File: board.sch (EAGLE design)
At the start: 130 parts, among them IC2 TPS61088RHLR, IC3 LMZ10501, Q1 IRFML8244TRPBF, Q2 IRFML8244TRPBF, Q3 IRFML8244TRPBF, Q4 IRFML8244TRPBF, Q5 IRFML8244TRPBF, U1 TB6612FNG, U3 STM32F405RG, U4 BMI088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

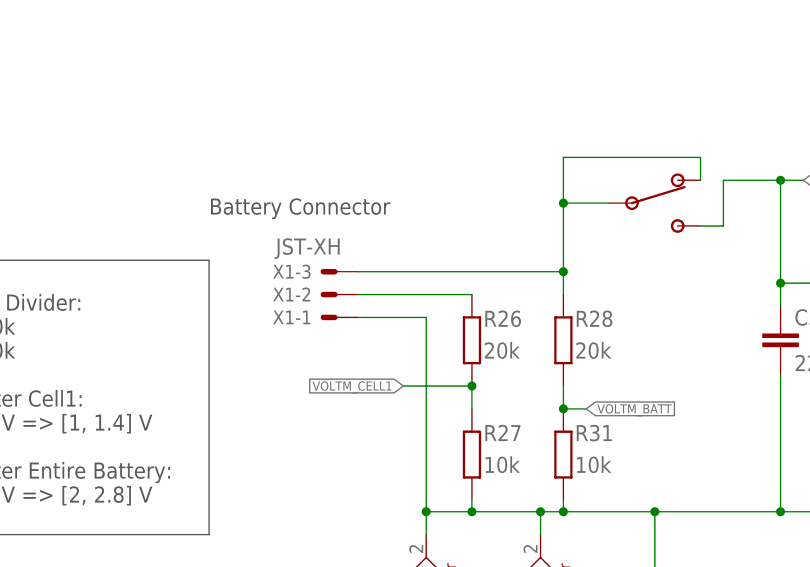
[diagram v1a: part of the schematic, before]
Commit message: 3D packages and footprint updates + board picture
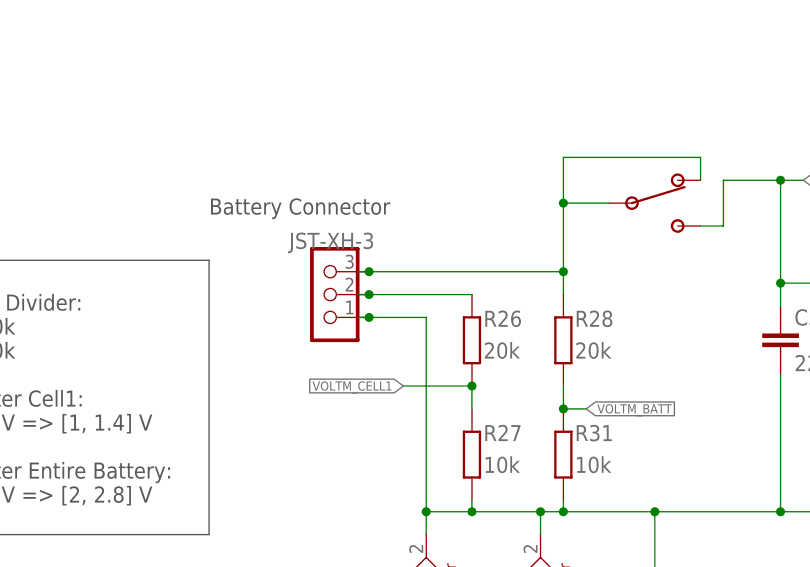
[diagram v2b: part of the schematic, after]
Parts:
- removed X1: JST-XH, JST XH Connectors:JST-XH-03-PIN-LONG-PAD
- added U$10: JST-XH-3, Isaks Bibliotek:JST-XH-3
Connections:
- net GND: now also U$10.1; no longer X1-1.S
- net N$33: now also U$10.2; no longer X1-2.S
- net N$38: now also U$10.3; no longer X1-3.S

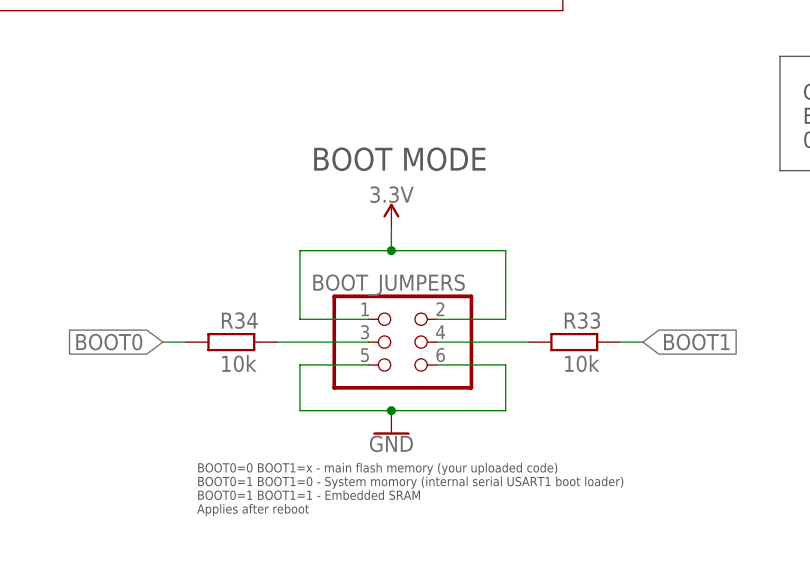
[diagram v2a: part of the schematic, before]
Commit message: 3D packages + component layout
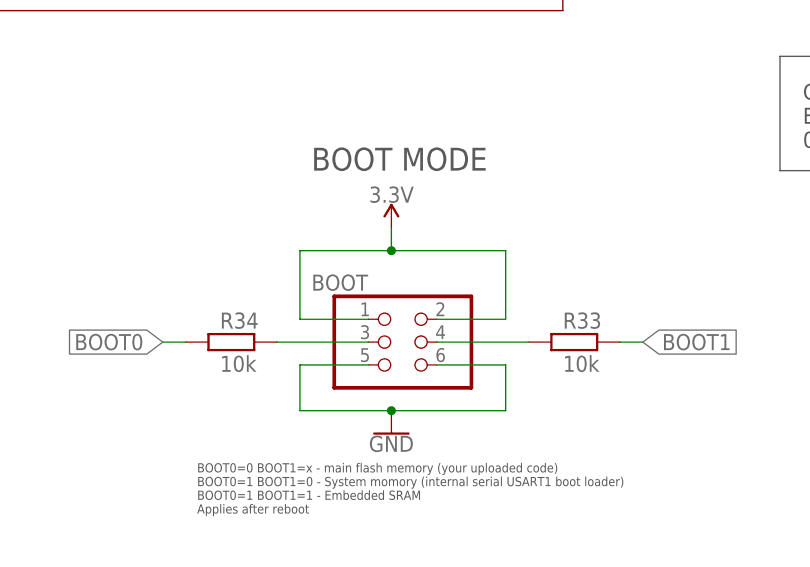
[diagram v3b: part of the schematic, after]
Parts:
- C31: RATING (none) -> X5R/X7R; V_RATING (none) -> 10V
- C32: RATING (none) -> X5R/X7R; V_RATING (none) -> 25V
- C33: V_RATING (none) -> 10v
- C_VC: RATING (none) -> X5R/X7R; V_RATING (none) -> 6.3V
- R23, RT: TOLERANCE (none) -> 1%
- renumbered BOOT_JUMPERS to BOOT
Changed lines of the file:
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@@
 <part name="R1" library="CASE-RCL" deviceset="R0603" device="" package3d_urn="urn:adsk.eagle:package:5332309/4" value="1.8k"/>
 <part name="R2" library="CASE-RCL" deviceset="R0603" device="" package3d_urn="urn:adsk.eagle:package:5332309/4" value="1.8k"/>
-<part name="RT" library="CASE-RCL" deviceset="R0603" device="" package3d_urn="urn:adsk.eagle:package:5332309/4" value="290k"/>
+<part name="RT" library="CASE-RCL" deviceset="R0603" device="" package3d_urn="urn:adsk.eagle:package:5332309/4" value="290k">
+<attribute name="TOLERANCE" value="1%"/>
+</part>
 <part name="RB" library="CASE-RCL" deviceset="R0603" device="" package3d_urn="urn:adsk.eagle:package:5332309/4" value="150k"/>
 <part name="C_IN" library="CASE-RCL" deviceset="C0805" device="" package3d_urn="urn:adsk.eagle:package:5332304/3" value="10u"/>
 <part name="C_OUT" library="CASE-RCL" deviceset="C0805" device="" package3d_urn="urn:adsk.eagle:package:5332304/3" value="10u"/>
-<part name="C_VC" library="CASE-RCL" deviceset="C0603" device="" package3d_urn="urn:adsk.eagle:package:5332305/5" value="470pF"/>
+<part name="C_VC" library="CASE-RCL" deviceset="C0603" device="" package3d_urn="urn:adsk.eagle:package:5332305/5" value="470pF">
+<attribute name="RATING" value="X5R/X7R"/>
+<attribute name="V_RATING" value="6.3V"/>
+</part>
 <part name="Q4" library="Isaks Bibliotek" library_urn="urn:adsk.eagle:library:11889733" deviceset="IRFML8244TRPBF" device="" package3d_urn="urn:adsk.eagle:package:12478112/1"/>
 <part name="Q3" library="Isaks Bibliotek" library_urn="urn:adsk.eagle:library:11889733" deviceset="IRFML8244TRPBF" device="" package3d_urn="urn:adsk.eagle:package:12478112/1"/>
@@
 <part name="S1" library="Isaks Bibliotek" library_urn="urn:adsk.eagle:library:11889733" deviceset="LMZ21701" device="" package3d_urn="urn:adsk.eagle:package:12971317/2"/>
 <part name="R_FBB" library="CASE-RCL" deviceset="R0603" device="" package3d_urn="urn:adsk.eagle:package:5332309/4" value="20k"/>
-<part name="C31" library="CASE-RCL" deviceset="C0603" device="" package3d_urn="urn:adsk.eagle:package:5332305/5" value="3300p"/>
+<part name="C31" library="CASE-RCL" deviceset="C0603" device="" package3d_urn="urn:adsk.eagle:package:5332305/5" value="3300p">
+<attribute name="RATING" value="X5R/X7R"/>
+<attribute name="V_RATING" value="10V"/>
+</part>
 <part name="GND21" library="Isaks Bibliotek" library_urn="urn:adsk.eagle:library:11889733" deviceset="GND" device=""/>
-<part name="C32" library="CASE-RCL" deviceset="C0805" device="" package3d_urn="urn:adsk.eagle:package:5332304/3" value="22u"/>
-<part name="R23" library="CASE-RCL" deviceset="R0603" device="" package3d_urn="urn:adsk.eagle:package:5332309/4" value="10k"/>
-<part name="C33" library="CASE-RCL" deviceset="C0805" device="" package3d_urn="urn:adsk.eagle:package:5332304/3" value="22u"/>
+<part name="C32" library="CASE-RCL" deviceset="C0805" device="" package3d_urn="urn:adsk.eagle:package:5332304/3" value="22u">
+<attribute name="RATING" value="X5R/X7R"/>
+<attribute name="V_RATING" value="25V"/>
+</part>
+<part name="R23" library="CASE-RCL" deviceset="R0603" device="" package3d_urn="urn:adsk.eagle:package:5332309/4" value="10k">
+<attribute name="TOLERANCE" value="1%"/>
+</part>
+<part name="C33" library="CASE-RCL" deviceset="C0805" device="" package3d_urn="urn:adsk.eagle:package:5332304/3" value="22u">
+<attribute name="V_RATING" value="10v"/>
+</part>
 <part name="SUPPLY14" library="Isaks Bibliotek" library_urn="urn:adsk.eagle:library:11889733" deviceset="5V" device=""/>
 <part name="R_FBT" library="CASE-RCL" deviceset="R0603" device="" package3d_urn="urn:adsk.eagle:package:5332309/4" value="105k"/>
@@
 <part name="GND34" library="Isaks Bibliotek" library_urn="urn:adsk.eagle:library:11889733" deviceset="GND" device=""/>
 <part name="SUPPLY27" library="Isaks Bibliotek" library_urn="urn:adsk.eagle:library:11889733" deviceset="3.3V" device=""/>
-<part name="BOOT_JUMPERS" library="CASE-Pinhead" deviceset="PINHD-2X3" device="" package3d_urn="urn:adsk.eagle:package:22462/2"/>
+<part name="BOOT" library="CASE-Pinhead" deviceset="PINHD-2X3" device="" package3d_urn="urn:adsk.eagle:package:22462/2"/>
 <part name="SUPPLY29" library="SparkFun-PowerSymbols" deviceset="3.3V" device=""/>
 <part name="GND36" library="SparkFun-PowerSymbols" deviceset="GND" device=""/>
@@
 <attribute name="NAME" x="173.99" y="288.0614" size="1.778" layer="95" rot="R180"/>
 <attribute name="VALUE" x="173.99" y="285.242" size="1.778" layer="96" rot="R180"/>
+<attribute name="TOLERANCE" x="176.53" y="285.75" size="1.778" layer="96" rot="R90" display="off"/>
 </instance>
 <instance part="RB" gate="G$1" x="176.53" y="270.51" smashed="yes" rot="R90" grouprefs="POWER_REGULATION">
@@
 <attribute name="NAME" x="161.036" y="273.939" size="1.778" layer="95" rot="R180"/>
 <attribute name="VALUE" x="162.306" y="268.859" size="1.778" layer="96" rot="R180"/>
+<attribute name="RATING" x="163.83" y="271.78" size="1.778" layer="96" display="off"/>
+<attribute name="V_RATING" x="163.83" y="271.78" size="1.778" layer="96" display="off"/>
 </instance>
 <instance part="Q4" gate="G$1" x="299.72" y="439.42" smashed="yes" grouprefs="EMITTERS">
@@
 <attribute name="NAME" x="124.714" y="348.361" size="1.778" layer="95"/>
 <attribute name="VALUE" x="124.714" y="343.281" size="1.778" layer="96"/>
+<attribute name="RATING" x="123.19" y="347.98" size="1.778" layer="96" display="off"/>
+<attribute name="V_RATING" x="123.19" y="347.98" size="1.778" layer="96" display="off"/>
 </instance>
 <instance part="GND21" gate="1" x="102.87" y="314.96" smashed="yes" grouprefs="POWER_REGULATION">
@@
 <attribute name="NAME" x="118.364" y="357.251" size="1.778" layer="95"/>
 <attribute name="VALUE" x="118.364" y="352.171" size="1.778" layer="96"/>
+<attribute name="RATING" x="116.84" y="356.87" size="1.778" layer="96" display="off"/>
+<attribute name="V_RATING" x="116.84" y="356.87" size="1.778" layer="96" display="off"/>
 </instance>
 <instance part="R23" gate="G$1" x="167.64" y="356.87" smashed="yes" rot="R90" grouprefs="POWER_REGULATION">
 <attribute name="NAME" x="170.18" y="358.3686" size="1.778" layer="95"/>
 <attribute name="VALUE" x="170.18" y="354.838" size="1.778" layer="96"/>
+<attribute name="TOLERANCE" x="167.64" y="356.87" size="1.778" layer="96" rot="R90" display="off"/>
 </instance>
 <instance part="C33" gate="G$1" x="196.85" y="356.87" smashed="yes" grouprefs="POWER_REGULATION">
 <attribute name="NAME" x="198.374" y="357.251" size="1.778" layer="95"/>
 <attribute name="VALUE" x="198.374" y="352.171" size="1.778" layer="96"/>
+<attribute name="V_RATING" x="196.85" y="356.87" size="1.778" layer="96" display="off"/>
 </instance>
 <instance part="SUPPLY14" gate="G$1" x="196.85" y="365.76" smashed="yes" grouprefs="POWER_REGULATION">
@@
 <attribute name="VALUE" x="525.78" y="322.834" size="1.778" layer="96" align="bottom-center"/>
 </instance>
-<instance part="BOOT_JUMPERS" gate="A" x="449.58" y="218.44" smashed="yes" grouprefs="MICROCONTROLLER">
+<instance part="BOOT" gate="A" x="449.58" y="218.44" smashed="yes" grouprefs="MICROCONTROLLER">
 <attribute name="NAME" x="440.69" y="224.155" size="1.778" layer="95"/>
 <attribute name="VALUE" x="443.23" y="210.82" size="1.778" layer="96"/>
@@
 </segment>
 <segment>
-<pinref part="BOOT_JUMPERS" gate="A" pin="5"/>
+<pinref part="BOOT" gate="A" pin="5"/>
 <wire x1="447.04" y1="215.9" x2="439.42" y2="215.9" width="0.1524" layer="91" grouprefs="MICROCONTROLLER"/>
 <wire x1="439.42" y1="215.9" x2="439.42" y2="210.82" width="0.1524" layer="91" grouprefs="MICROCONTROLLER"/>
 <wire x1="439.42" y1="210.82" x2="449.58" y2="210.82" width="0.1524" layer="91" grouprefs="MICROCONTROLLER"/>
 <pinref part="GND36" gate="1" pin="GND"/>
-<pinref part="BOOT_JUMPERS" gate="A" pin="6"/>
+<pinref part="BOOT" gate="A" pin="6"/>
 <wire x1="454.66" y1="215.9" x2="462.28" y2="215.9" width="0.1524" layer="91" grouprefs="MICROCONTROLLER"/>
 <wire x1="462.28" y1="215.9" x2="462.28" y2="210.82" width="0.1524" layer="91" grouprefs="MICROCONTROLLER"/>
@@
 </segment>
 <segment>
-<pinref part="BOOT_JUMPERS" gate="A" pin="1"/>
+<pinref part="BOOT" gate="A" pin="1"/>
 <wire x1="447.04" y1="220.98" x2="439.42" y2="220.98" width="0.1524" layer="91" grouprefs="MICROCONTROLLER"/>
 <wire x1="439.42" y1="220.98" x2="439.42" y2="228.6" width="0.1524" layer="91" grouprefs="MICROCONTROLLER"/>
 <wire x1="439.42" y1="228.6" x2="449.58" y2="228.6" width="0.1524" layer="91" grouprefs="MICROCONTROLLER"/>
 <wire x1="449.58" y1="228.6" x2="449.58" y2="231.14" width="0.1524" layer="91" grouprefs="MICROCONTROLLER"/>
-<pinref part="BOOT_JUMPERS" gate="A" pin="2"/>
+<pinref part="BOOT" gate="A" pin="2"/>
 <wire x1="454.66" y1="220.98" x2="462.28" y2="220.98" width="0.1524" layer="91" grouprefs="MICROCONTROLLER"/>
 <wire x1="462.28" y1="220.98" x2="462.28" y2="228.6" width="0.1524" layer="91" grouprefs="MICROCONTROLLER"/>
@@
 <net name="N$32" class="0">
 <segment>
-<pinref part="BOOT_JUMPERS" gate="A" pin="4"/>
+<pinref part="BOOT" gate="A" pin="4"/>
 <wire x1="454.66" y1="218.44" x2="464.82" y2="218.44" width="0.1524" layer="91" grouprefs="MICROCONTROLLER"/>
 <pinref part="R33" gate="G$1" pin="2"/>
@@
 <net name="N$34" class="0">
 <segment>
-<pinref part="BOOT_JUMPERS" gate="A" pin="3"/>
+<pinref part="BOOT" gate="A" pin="3"/>
 <wire x1="447.04" y1="218.44" x2="436.88" y2="218.44" width="0.1524" layer="91" grouprefs="MICROCONTROLLER"/>
 <pinref part="R34" gate="G$1" pin="1"/>

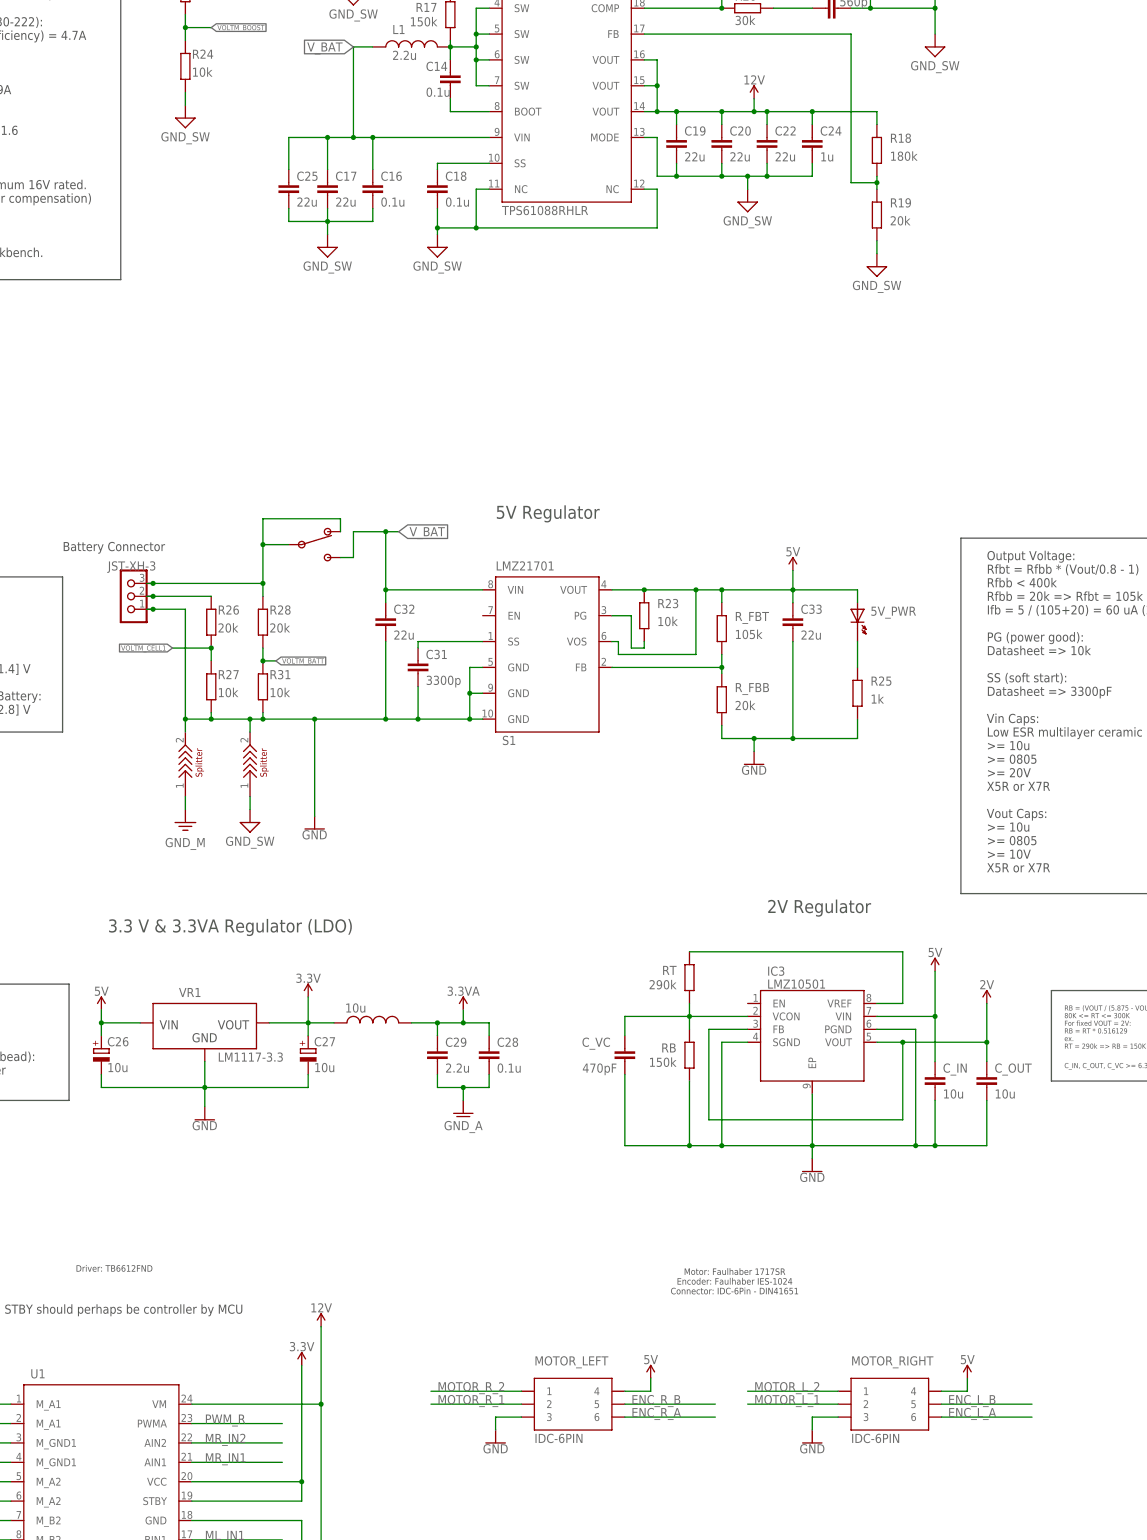
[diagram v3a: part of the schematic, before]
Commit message: Routing power
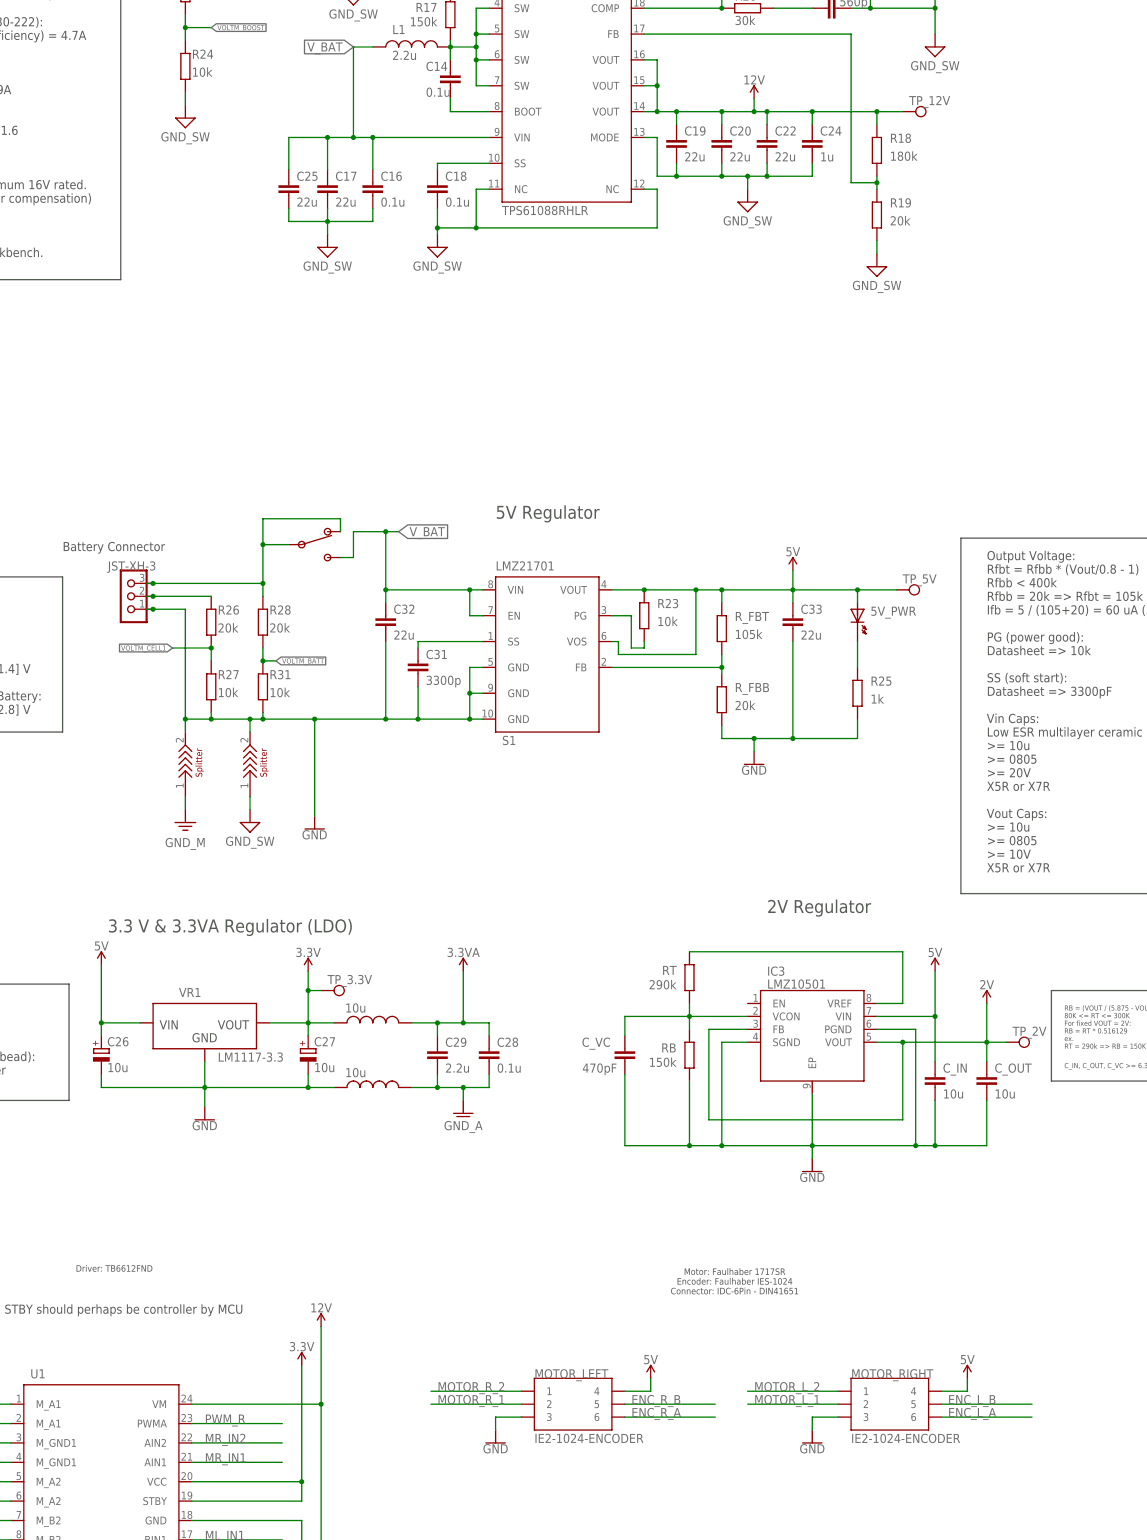
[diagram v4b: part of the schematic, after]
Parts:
- added FP2: 10u, CASE-RCL:WE-CBF_0805
- added TP_12V, TP_2V, TP_3.3V, TP_5V: TEST-POINT3X5, Isaks Bibliotek:TEST-POINT3X5
- MOTOR_LEFT, MOTOR_RIGHT: value IDC-6PIN -> IE2-1024-ENCODER; device Isaks Bibliotek:IDC-6PIN -> Isaks Bibliotek:IE2-1024-ENCODER
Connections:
- net 12V: now also TP_12V.1
- net 2V: now also TP_2V.1
- net 3.3V: now also TP_3.3V.1
- net 5V: now also TP_5V.1
- net GND: now also FP2.1
- net GND_A: now also FP2.2
- net V_BAT: now also S1.EN
